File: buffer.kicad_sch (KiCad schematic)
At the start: 22 parts, among them U1501 OPA1662AIDGKRQ1

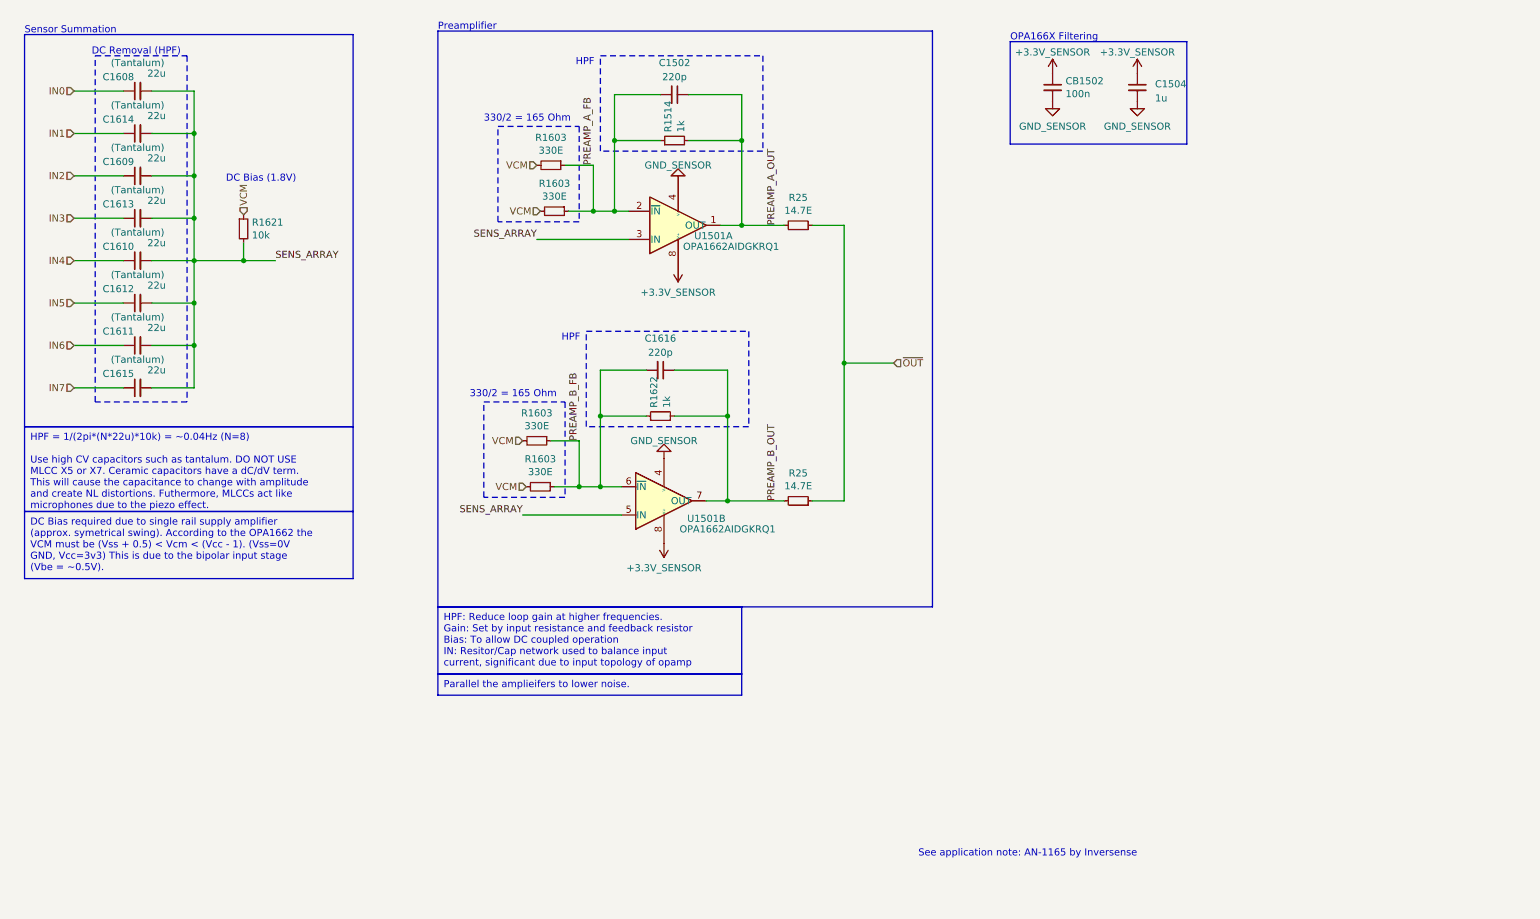
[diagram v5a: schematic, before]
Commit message: (sch) annotate summation stage
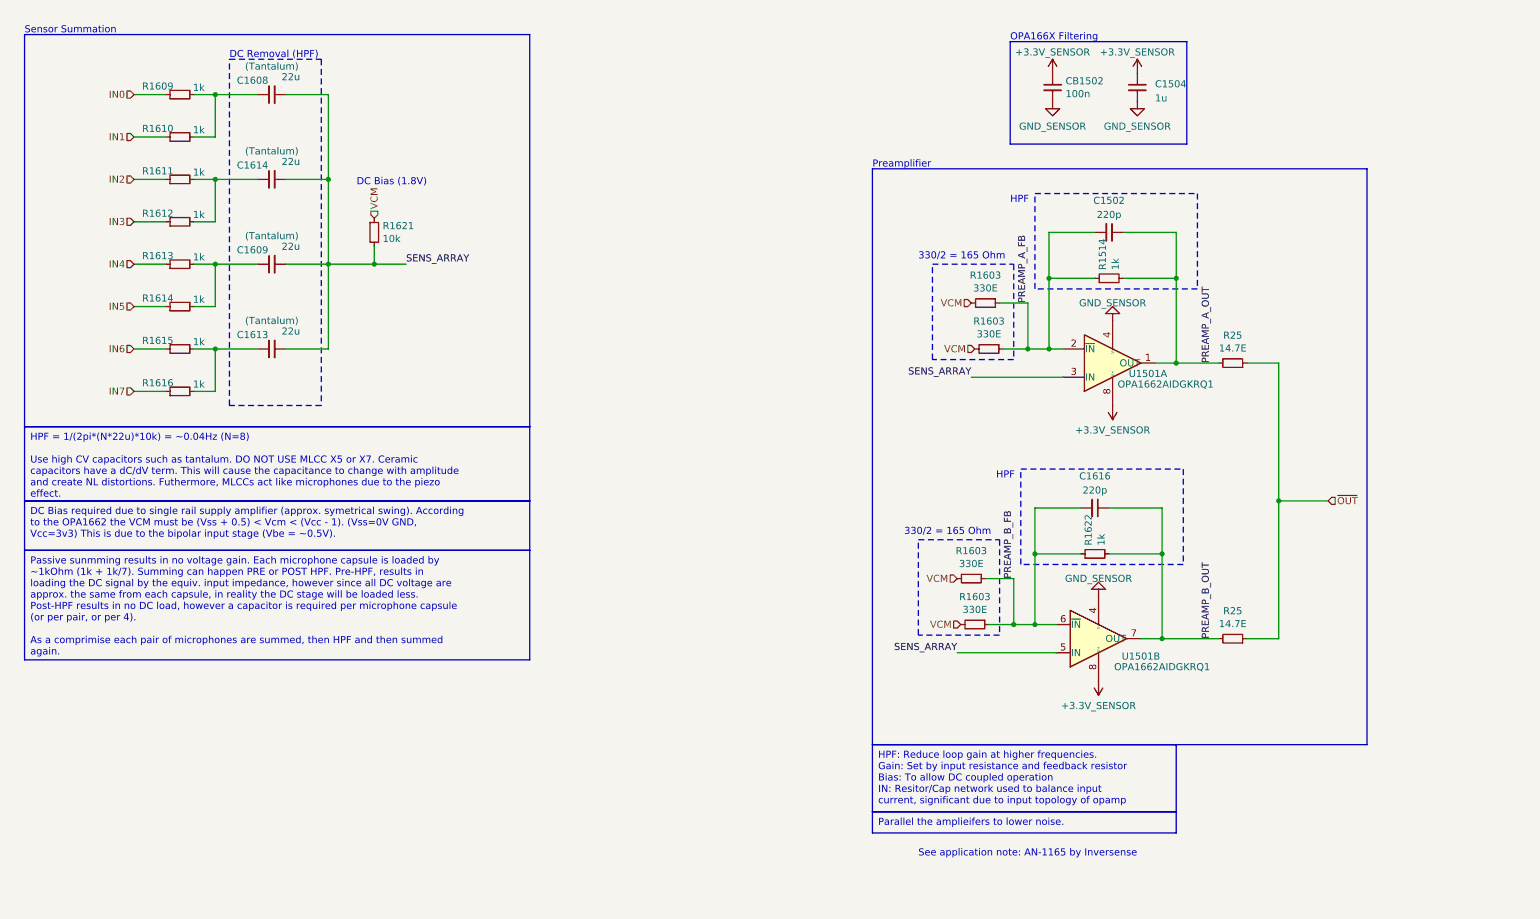
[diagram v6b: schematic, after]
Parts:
- removed C1610, C1611, C1612, C1615: 22u, Capacitor_Tantalum_SMD:CP_EIA-1608-10_AVX-L, symbol Device:C_Small
- added R1609, R1610, R1611, R1612, R1613, R1614, R1615, R1616: 1k, Resistor_SMD:R_0402_1005Metric, symbol Device:R_Small
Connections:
- net IN0: now also R1609.1; no longer C1608.1
- net IN1: now also R1610.1; no longer C1614.1
- net IN2: now also R1611.1; no longer C1609.1
- net IN3: now also R1612.1; no longer C1613.1
- net IN4: now also R1613.1
- net IN5: now also R1614.1
- net IN6: now also R1615.1
- net IN7: now also R1616.1
- new net: C1609.1, R1613.2, R1614.2
- new net: C1613.1, R1615.2, R1616.2
- new net: C1614.1, R1611.2, R1612.2
- new net: C1608.1, R1609.2, R1610.2
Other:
- moved on the sheet: C1502, C1608, C1609, C1613, C1614, C1616, R1514, R1603, R1621, R1622, R25, U1501A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

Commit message: (sch) change to OPA1664
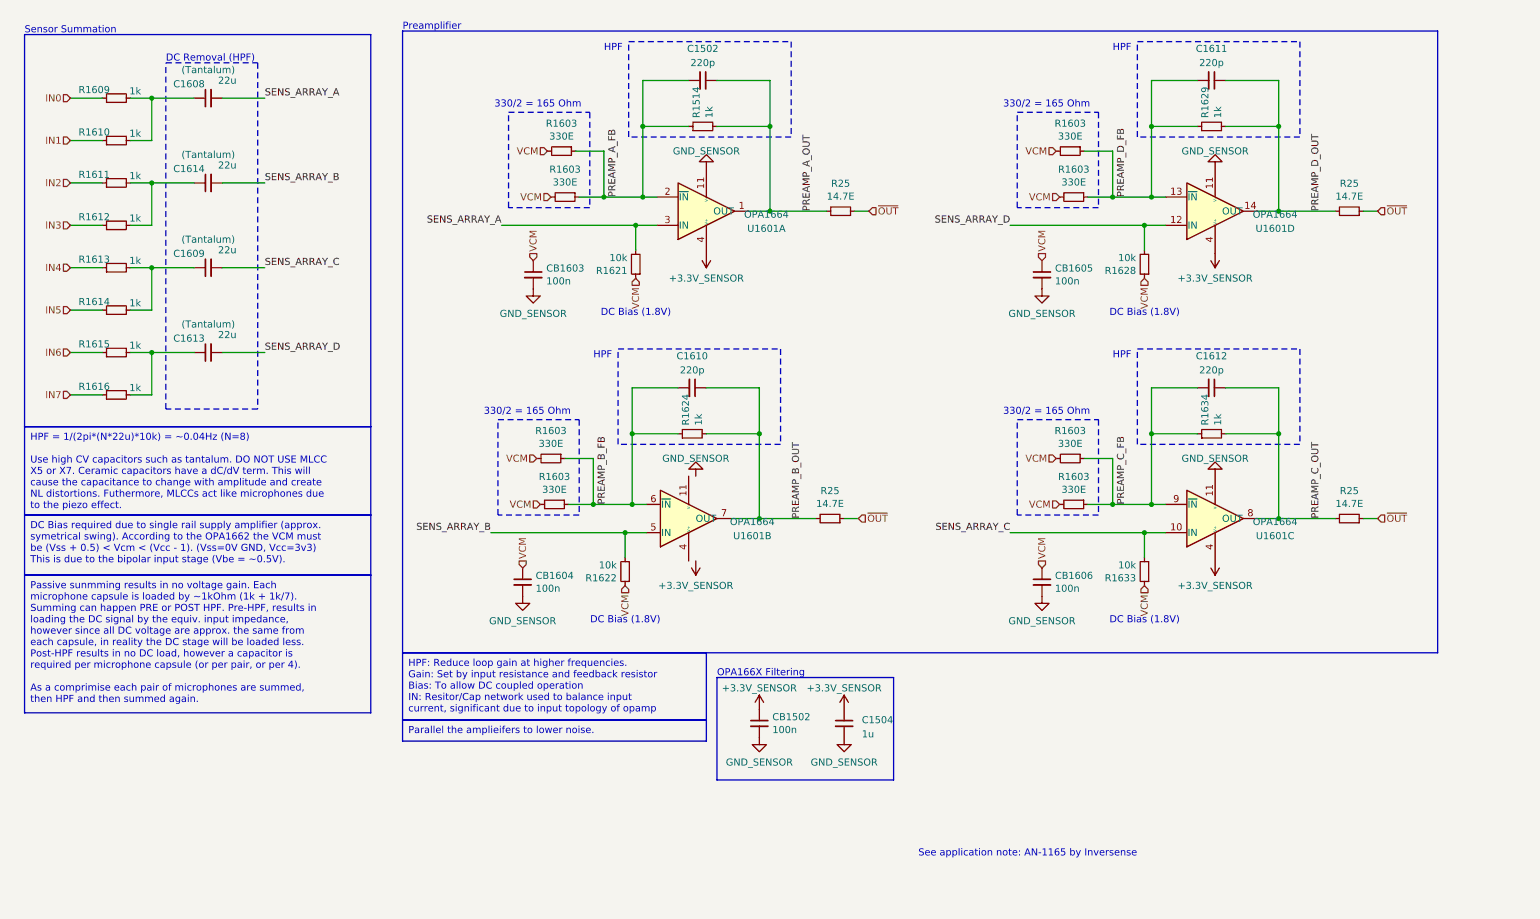
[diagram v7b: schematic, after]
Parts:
- removed C1616: 220p, Capacitor_SMD:C_0402_1005Metric, symbol Device:C_Small
- removed R1603 (x2): 330E, Resistor_SMD:R_0402_1005Metric, symbol Device:R_Small
- removed R25: 14.7E, Resistor_SMD:R_0402_1005Metric, symbol Device:R_Small
- removed U1501: OPA1662AIDGKRQ1, grootvoet:OPA1662AIDGK, symbol grootvoet:OPA1662
- added C1610, C1611, C1612: 220p, Capacitor_SMD:C_0402_1005Metric, symbol Device:C_Small
- added CB1603, CB1604, CB1605, CB1606: 100n, Capacitor_SMD:C_0402_1005Metric, symbol Device:C_Small
- added R1603 (x6): 330E, Resistor_SMD:R_0402_1005Metric, symbol Device:R_Small
- added R1624, R1629, R1634: 1k, Resistor_SMD:R_0402_1005Metric, symbol Device:R_Small
- added R1628, R1633: 10k, Resistor_SMD:R_0402_1005Metric, symbol Device:R_Small
- added R25 (x3): 14.7E, Resistor_SMD:R_0402_1005Metric, symbol Device:R_Small
- added U1601: OPA1664, grootvoet:Texas_PW_R-PDSO-G14, symbol grootvoet:OPA1664
- R1622: value 1k -> 10k; MPN RT0402FRE071KL -> (none)
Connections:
- net +3.3V: now also U1601.4 (V+), U1601.4 (V+), U1601.4 (V+)
- net GND: now also CB1603.2, CB1604.2, CB1605.2, CB1606.2, U1601.11 (V-), U1601.11 (V-), U1601.11 (V-)
- net PREAMP_A_FB: now also U1601.2 (~{IN})
- net PREAMP_A_OUT: now also U1601.1 (OUT)
- net PREAMP_B_FB: now also C1610.2, R1603.1, R1603.1, R1624.1, U1601.6 (~{IN}); no longer R1622.1
- net PREAMP_B_OUT: now also C1610.1, R1624.2, R25.2, U1601.7 (OUT); no longer R1622.2
- net VCM: now also R1622.1, CB1603.1, CB1604.1, CB1605.1, CB1606.1, R1603.2, R1603.2, R1603.2, R1603.2, R1603.2, R1603.2, R1628.1, R1633.1
- net ~{OUT}: now also R25.1, R25.1, R25.1
- removed net SENS_ARRAY: C1608.2, C1609.2, C1613.2, C1614.2, R1621.2
- new net PREAMP_C_FB: C1612.2, R1603.1, R1603.1, R1634.1, U1601.9 (~{IN})
- new net PREAMP_C_OUT: C1612.1, R1634.2, R25.2, U1601.8 (OUT)
- new net PREAMP_D_FB: C1611.2, R1603.1, R1603.1, R1629.1, U1601.13 (~{IN})
- new net PREAMP_D_OUT: C1611.1, R1629.2, R25.2, U1601.14 (OUT)
- new net SENS_ARRAY_A: C1608.2, R1621.2, U1601.3 (IN)
- new net SENS_ARRAY_B: C1614.2, R1622.2, U1601.5 (IN)
- new net SENS_ARRAY_C: C1609.2, R1633.2, U1601.10 (IN)
- new net SENS_ARRAY_D: C1613.2, R1628.2, U1601.12 (IN)
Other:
- moved on the sheet: C1502, C1504, C1608, C1609, C1613, C1614, CB1502, R1514, R1603, R1609, R1610, R1611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

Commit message: (pcb) layout summing out
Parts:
- added CB1607, CB1608, CB1609, CB1610: 100n, Capacitor_SMD:C_0402_1005Metric, symbol Device:C_Small
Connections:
- net GND: now also CB1607.2, CB1608.2, CB1609.2, CB1610.2
- net VCM: now also CB1607.1, CB1608.1, CB1609.1, CB1610.1
